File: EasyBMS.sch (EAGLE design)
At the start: 147 parts, among them Q1 BSS308PEH6327XTSA1, Q10 BSS308PEH6327XTSA1, Q11 BSS308PEH6327XTSA1, Q12 BSS308PEH6327XTSA1, Q14 BSS308PEH6327XTSA1, Q3 BSS308PEH6327XTSA1, Q4 BSS308PEH6327XTSA1, Q5 BSS308PEH6327XTSA1, Q6 BSS308PEH6327XTSA1, Q7 BSS308PEH6327XTSA1, Q8 BSS308PEH6327XTSA1, Q9 BSS308PEH6327XTSA1

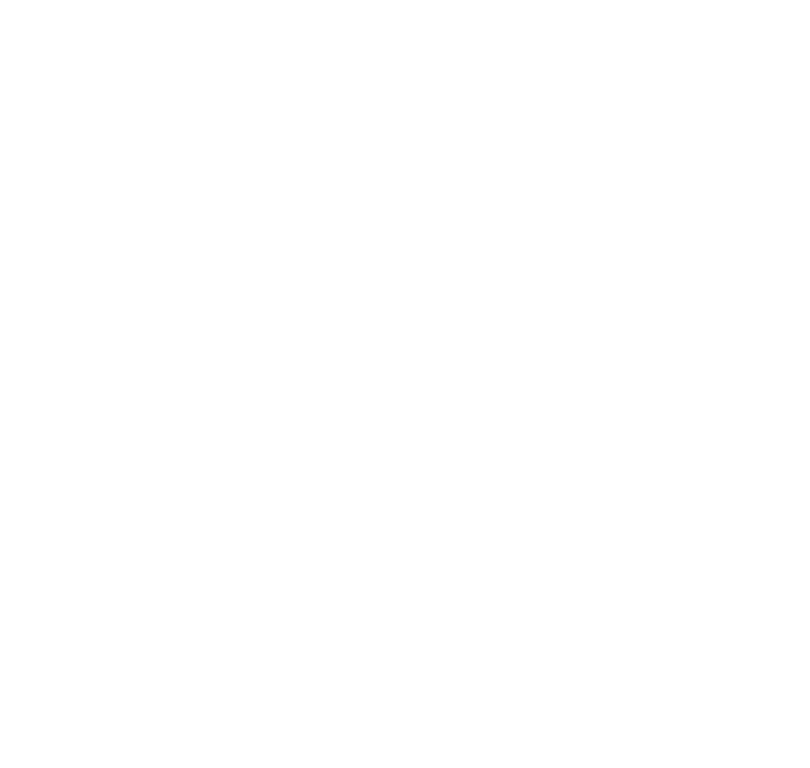
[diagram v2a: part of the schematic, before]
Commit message: shortconnection pinable between the C ports for emtpy cells
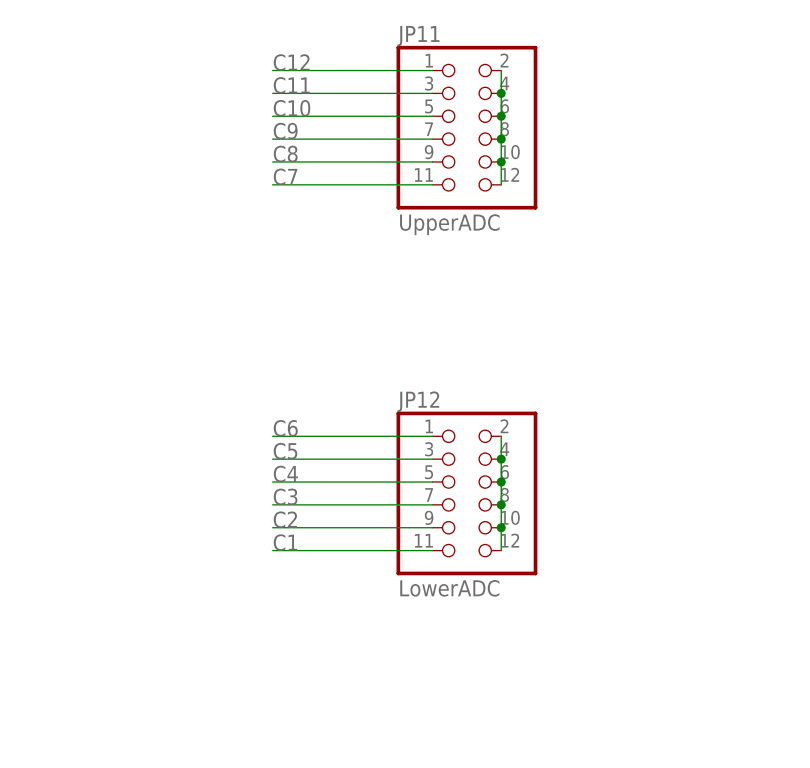
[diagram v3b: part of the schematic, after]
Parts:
- added JP11: UpperADC, pinhead:PINHD-2X6
- added JP12: LowerADC, pinhead:PINHD-2X6
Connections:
- new net N$106: JP12.10, JP12.12, JP12.2, JP12.4, JP12.6, JP12.8
- new net N$121: JP11.10, JP11.12, JP11.2, JP11.4, JP11.6, JP11.8
- net C1: now also JP12.11
- net C10: now also JP11.5
- net C11: now also JP11.3
- net C12: now also JP11.1
- net C2: now also JP12.9
- net C3: now also JP12.7
- net C4: now also JP12.5
- net C5: now also JP12.3
- net C6: now also JP12.1
- net C7: now also JP11.11
- net C8: now also JP11.9
- net C9: now also JP11.7
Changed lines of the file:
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@@
 <part name="D2" library="SamacSys_Parts" deviceset="SM4007PL-TP" device=""/>
 <part name="D3" library="SamacSys_Parts" deviceset="SM4007PL-TP" device=""/>
+<part name="JP11" library="pinhead" library_urn="urn:adsk.eagle:library:325" deviceset="PINHD-2X6" device="" package3d_urn="urn:adsk.eagle:package:22474/2" value="UpperADC"/>
+<part name="JP12" library="pinhead" library_urn="urn:adsk.eagle:library:325" deviceset="PINHD-2X6" device="" package3d_urn="urn:adsk.eagle:package:22474/2" value="LowerADC"/>
 </parts>
 <sheets>
@@
 <attribute name="NAME" x="-414.02" y="69.85" size="1.778" layer="95" rot="R270" align="center-left"/>
 <attribute name="VALUE" x="-416.56" y="69.85" size="1.778" layer="96" rot="R270" align="center-left"/>
+</instance>
+<instance part="JP11" gate="A" x="-50.8" y="726.44" smashed="yes">
+<attribute name="NAME" x="-57.15" y="734.695" size="1.778" layer="95"/>
+<attribute name="VALUE" x="-57.15" y="713.74" size="1.778" layer="96"/>
+</instance>
+<instance part="JP12" gate="A" x="-50.8" y="685.8" smashed="yes">
+<attribute name="NAME" x="-57.15" y="694.055" size="1.778" layer="95"/>
+<attribute name="VALUE" x="-57.15" y="673.1" size="1.778" layer="96"/>
 </instance>
 </instances>
@@
 <label x="-180.34" y="86.36" size="1.778" layer="95"/>
 </segment>
+<segment>
+<pinref part="JP12" gate="A" pin="11"/>
+<wire x1="-53.34" y1="678.18" x2="-71.12" y2="678.18" width="0.1524" layer="91"/>
+<label x="-71.12" y="678.18" size="1.778" layer="95"/>
+</segment>
 </net>
 <net name="S2" class="0">
@@
 <label x="-180.34" y="137.16" size="1.778" layer="95"/>
 </segment>
+<segment>
+<pinref part="JP12" gate="A" pin="9"/>
+<wire x1="-53.34" y1="680.72" x2="-71.12" y2="680.72" width="0.1524" layer="91"/>
+<label x="-71.12" y="680.72" size="1.778" layer="95"/>
+</segment>
 </net>
 <net name="S3" class="0">
@@
 <label x="-180.34" y="182.88" size="1.778" layer="95"/>
 </segment>
+<segment>
+<pinref part="JP12" gate="A" pin="7"/>
+<wire x1="-53.34" y1="683.26" x2="-71.12" y2="683.26" width="0.1524" layer="91"/>
+<label x="-71.12" y="683.26" size="1.778" layer="95"/>
+</segment>
 </net>
 <net name="S4" class="0">
@@
 <label x="-180.34" y="231.14" size="1.778" layer="95"/>
 </segment>
+<segment>
+<pinref part="JP12" gate="A" pin="5"/>
+<wire x1="-53.34" y1="685.8" x2="-71.12" y2="685.8" width="0.1524" layer="91"/>
+<label x="-71.12" y="685.8" size="1.778" layer="95"/>
+</segment>
 </net>
 <net name="S5" class="0">
@@
 <label x="-180.34" y="276.86" size="1.778" layer="95"/>
 </segment>
+<segment>
+<pinref part="JP12" gate="A" pin="3"/>
+<wire x1="-53.34" y1="688.34" x2="-71.12" y2="688.34" width="0.1524" layer="91"/>
+<label x="-71.12" y="688.34" size="1.778" layer="95"/>
+</segment>
 </net>
 <net name="S6" class="0">
@@
 <label x="-180.34" y="320.04" size="1.778" layer="95"/>
 </segment>
+<segment>
+<pinref part="JP12" gate="A" pin="1"/>
+<wire x1="-53.34" y1="690.88" x2="-71.12" y2="690.88" width="0.1524" layer="91"/>
+<label x="-71.12" y="690.88" size="1.778" layer="95"/>
+</segment>
 </net>
 <net name="S7" class="0">
@@
 <label x="-180.34" y="363.22" size="1.778" layer="95"/>
 </segment>
+<segment>
+<pinref part="JP11" gate="A" pin="11"/>
+<wire x1="-53.34" y1="718.82" x2="-71.12" y2="718.82" width="0.1524" layer="91"/>
+<label x="-71.12" y="718.82" size="1.778" layer="95"/>
+</segment>
 </net>
 <net name="S8" class="0">
@@
 <label x="-180.34" y="414.02" size="1.778" layer="95"/>
 </segment>
+<segment>
+<pinref part="JP11" gate="A" pin="9"/>
+<wire x1="-53.34" y1="721.36" x2="-71.12" y2="721.36" width="0.1524" layer="91"/>
+<label x="-71.12" y="721.36" size="1.778" layer="95"/>
+</segment>
 </net>
 <net name="S9" class="0">
@@
 <label x="-180.34" y="459.74" size="1.778" layer="95"/>
 </segment>
+<segment>
+<pinref part="JP11" gate="A" pin="7"/>
+<wire x1="-53.34" y1="723.9" x2="-71.12" y2="723.9" width="0.1524" layer="91"/>
+<label x="-71.12" y="723.9" size="1.778" layer="95"/>
+</segment>
 </net>
 <net name="S10" class="0">
@@
 <label x="-180.34" y="502.92" size="1.778" layer="95"/>
 </segment>
+<segment>
+<pinref part="JP11" gate="A" pin="5"/>
+<wire x1="-53.34" y1="726.44" x2="-71.12" y2="726.44" width="0.1524" layer="91"/>
+<label x="-71.12" y="726.44" size="1.778" layer="95"/>
+</segment>
 </net>
 <net name="S11" class="0">
@@
 <label x="-180.34" y="551.18" size="1.778" layer="95"/>
 </segment>
+<segment>
+<pinref part="JP11" gate="A" pin="3"/>
+<wire x1="-53.34" y1="728.98" x2="-71.12" y2="728.98" width="0.1524" layer="91"/>
+<label x="-71.12" y="728.98" size="1.778" layer="95"/>
+</segment>
 </net>
 <net name="S12" class="0">
@@
 <pinref part="R81" gate="G$1" pin="1"/>
 <label x="-180.34" y="596.9" size="1.778" layer="95"/>
+</segment>
+<segment>
+<pinref part="JP11" gate="A" pin="1"/>
+<wire x1="-53.34" y1="731.52" x2="-71.12" y2="731.52" width="0.1524" layer="91"/>
+<label x="-71.12" y="731.52" size="1.778" layer="95"/>
 </segment>
 </net>
@@
 </segment>
 </net>
+<net name="N$106" class="0">
+<segment>
+<pinref part="JP12" gate="A" pin="2"/>
+<pinref part="JP12" gate="A" pin="4"/>
+<wire x1="-45.72" y1="690.88" x2="-45.72" y2="688.34" width="0.1524" layer="91"/>
+<pinref part="JP12" gate="A" pin="6"/>
+<wire x1="-45.72" y1="688.34" x2="-45.72" y2="685.8" width="0.1524" layer="91"/>
+<junction x="-45.72" y="688.34"/>
+<pinref part="JP12" gate="A" pin="8"/>
+<wire x1="-45.72" y1="685.8" x2="-45.72" y2="683.26" width="0.1524" layer="91"/>
+<junction x="-45.72" y="685.8"/>
+<pinref part="JP12" gate="A" pin="10"/>
+<wire x1="-45.72" y1="683.26" x2="-45.72" y2="680.72" width="0.1524" layer="91"/>
+<junction x="-45.72" y="683.26"/>
+<pinref part="JP12" gate="A" pin="12"/>
+<wire x1="-45.72" y1="680.72" x2="-45.72" y2="678.18" width="0.1524" layer="91"/>
+<junction x="-45.72" y="680.72"/>
+</segment>
+</net>
+<net name="N$121" class="0">
+<segment>
+<pinref part="JP11" gate="A" pin="2"/>
+<pinref part="JP11" gate="A" pin="4"/>
+<wire x1="-45.72" y1="731.52" x2="-45.72" y2="728.98" width="0.1524" layer="91"/>
+<pinref part="JP11" gate="A" pin="6"/>
+<wire x1="-45.72" y1="728.98" x2="-45.72" y2="726.44" width="0.1524" layer="91"/>
+<junction x="-45.72" y="728.98"/>
+<pinref part="JP11" gate="A" pin="8"/>
+<wire x1="-45.72" y1="726.44" x2="-45.72" y2="723.9" width="0.1524" layer="91"/>
+<junction x="-45.72" y="726.44"/>
+<pinref part="JP11" gate="A" pin="10"/>
+<wire x1="-45.72" y1="723.9" x2="-45.72" y2="721.36" width="0.1524" layer="91"/>
+<junction x="-45.72" y="723.9"/>
+<pinref part="JP11" gate="A" pin="12"/>
+<wire x1="-45.72" y1="721.36" x2="-45.72" y2="718.82" width="0.1524" layer="91"/>
+<junction x="-45.72" y="721.36"/>
+</segment>
+</net>

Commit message: some caps got new values
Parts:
- added C16, C21: 100nF, rcl:C-EUC1206
- added R4: 100R, rcl:R-EU_R0402
- C10, C11, C12, C13, C14, C15, C17, C4, C5, C6, C7, C8, C9: value (none) -> 10nF
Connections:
- new net V+: C21.1, JP5.1, R4.1
- net GND: now also C16.2, C21.2
- net P13: now also R4.2; no longer JP5.1
- net VREG: now also C16.1
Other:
- moved on the sheet: C1, C10, C11, C12, C13, C14, C15, C17, C2, C3, C4, C5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

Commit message: MOSFETS changed to a available Type
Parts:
- added C18, C19: 100nF, rcl:C-EUC1206
- Q1, Q10, Q11, Q12, Q14, Q3, Q4, Q5, Q6, Q7, Q8, Q9: value BSS308PEH6327XTSA1 -> C8547
- R5: device rcl:R-EU_R0603 -> rcl:R-EU_R0402
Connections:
- net 5VDC: no longer C3.+
- net GND: now also C18.2, C19.2
- net VREF1: now also C18.1
- net VREF2: now also C19.1
- net VREG: now also C3.+
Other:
- moved on the sheet: C1, C3

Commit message: layouted
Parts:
- removed C6: 10nF, rcl:C-EUC0402
- removed LED18, LED6: KT-0603R, led:LEDCHIPLED_0603
- removed Q14, Q3: C8547, SamacSys_Parts:BSS308PEH6327XTSA1
- removed R100, R23: 100R, rcl:R-EU_R0402
- removed R12, R14, R20, R97: 10R0, rcl:R-EU_R1206
- removed R21, R98: 3.3k, rcl:R-EU_R0402
- removed R22, R99: 470R, rcl:R-EU_R0402
- added C20: 10nF, rcl:C-EUC0402
- added LED17, LED5: KT-0603R, led:LEDCHIPLED_0603
- added Q13, Q2: C8547, SamacSys_Parts:BSS308PEH6327XTSA1
- added R10, R94: 3.3k, rcl:R-EU_R0402
- added R11, R89: 470R, rcl:R-EU_R0402
- added R7, R8, R91, R92, R93: 10R0, rcl:R-EU_R1206
- added R90: 100R, rcl:R-EU_R0402
- R13: value 3.3k -> 100R
- R19, R29, R35, R41, R47, R63, R69, R75, R81: value 100R -> 10R0; device rcl:R-EU_R0402 -> rcl:R-EU_R1206
- R24, R30, R36, R42, R48, R64, R70, R76: value 10R0 -> 3.3k; device rcl:R-EU_R1206 -> rcl:R-EU_R0402
- R25, R31, R37, R43, R49, R65, R71, R77, R83, R95: value 10R0 -> 470R; device rcl:R-EU_R1206 -> rcl:R-EU_R0402
- R26, R32, R38, R44, R50, R66, R72, R78, R84, R96: value 10R0 -> 100R; device rcl:R-EU_R1206 -> rcl:R-EU_R0402
- R27, R33, R39, R45, R51, R67, R73, R79, R86: value 3.3k -> 10R0; device rcl:R-EU_R0402 -> rcl:R-EU_R1206
- R28, R34, R40, R46, R52, R68, R74, R80, R87: value 470R -> 10R0; device rcl:R-EU_R0402 -> rcl:R-EU_R1206
- R82: value 470R -> 3.3k
- R88: value 100R -> 3.3k
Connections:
- removed net N$14: R12.2, R14.1
- removed net N$15: R18.2, R9.1
- removed net N$157: LED10.C, R82.1
- removed net N$16: R14.2, R20.1
- removed net N$19: LED6.A, Q3.D, R20.2
- removed net N$20: Q3.G, R21.2
- removed net N$22: LED6.C, R22.1
- removed net N$27 (its old number): LED7.A, Q4.D, R26.2
- new net N$122: Q12.G, R88.2
- new net N$123: LED16.C, R89.1
- new net N$125: R91.2, R92.1
- new net N$126: R92.2, R93.1
- new net N$127: LED17.A, Q13.D, R93.2
- new net N$128: Q13.G, R94.2
- new net N$129: LED17.C, R95.1
- new net N$17: R7.2, R8.1
- net C1: now also R13.1; no longer R19.1
- net C10: now also C15.1, R84.1; no longer C17.1, R100.1
- net C11: now also C17.1, R90.1; no longer C12.1, R69.1
- net C12: now also C20.1, R96.1; no longer C14.1, R81.1
- net C2: now also C8.1, R32.1; no longer C6.1, R23.1
- net C3: now also R26.1; no longer R29.1
- net C4: now also C9.1, R38.1; no longer C8.1, R35.1
- net C5: now also C10.1, R44.1; no longer C9.1, R41.1
- net C6: now also C11.1, R50.1; no longer C10.1, R47.1
- net C7: now also C12.1, R66.1; no longer C11.1, R63.1
- net C8: now also R72.1; no longer R75.1
- net C9: now also C14.1, R78.1; no longer C15.1, R88.1
- net GND: now also R11.2, R7.1; no longer R17.1, R82.2
- net N$18: now also R8.2, R9.1; no longer LED10.A, Q1.D, R9.2
- net N$23: now also LED5.A, Q1.D, R9.2; no longer R24.2, R25.1
- net N$25: now also R10.2; no longer R13.2
- net N$26: now also LED5.C, R11.1; no longer R25.2, R26.1
- net N$28: now also R18.2, R19.1; no longer Q4.G, R27.2
- net N$29: now also LED7.A, Q2.D, R19.2; no longer LED7.C, R28.1
- net N$31: now also Q2.G, R24.2; no longer R30.2, R31.1
- net N$32: now also LED7.C, R25.1; no longer R31.2, R32.1
- net N$33: now also R27.2, R28.1; no longer LED8.A, Q5.D, R32.2
- net N$34: now also R28.2, R29.1; no longer Q5.G, R33.2
- net N$35: now also LED8.A, Q4.D, R29.2; no longer LED8.C, R34.1
- net N$36: now also Q4.G, R30.2; no longer R36.2, R37.1
- net N$37: now also LED8.C, R31.1; no longer R37.2, R38.1
- net N$38: now also R33.2, R34.1; no longer LED9.A, Q6.D, R38.2
- net N$39: now also R34.2, R35.1; no longer Q6.G, R39.2
- net N$40: now also LED9.A, Q5.D, R35.2; no longer LED9.C, R40.1
- net N$41: now also Q5.G, R36.2; no longer R42.2, R43.1
- net N$42: now also LED9.C, R37.1; no longer R43.2, R44.1
- net N$43: now also R39.2, R40.1; no longer LED11.A, Q7.D, R44.2
- net N$44: now also R40.2, R41.1; no longer Q7.G, R45.2
- net N$45: now also LED10.A, Q6.D, R41.2; no longer LED11.C, R46.1
- net N$46: now also Q6.G, R42.2; no longer R48.2, R49.1
- net N$47: now also LED10.C, R43.1; no longer R49.2, R50.1
- net N$48: now also R45.2, R46.1; no longer LED12.A, Q8.D, R50.2
- net N$49: now also R46.2, R47.1; no longer Q8.G, R51.2
- net N$50: now also LED11.A, Q7.D, R47.2; no longer LED12.C, R52.1
- net N$51: now also Q7.G, R48.2; no longer R64.2, R65.1
- net N$52: now also LED11.C, R49.1; no longer R65.2, R66.1
- net N$53: now also R51.2, R52.1; no longer LED13.A, Q9.D, R66.2
- net N$54: now also R52.2, R63.1; no longer Q9.G, R67.2
- net N$55: now also LED12.A, Q8.D, R63.2; no longer LED13.C, R68.1
- net N$56: now also Q8.G, R64.2; no longer R70.2, R71.1
- net N$57: now also LED12.C, R65.1; no longer R71.2, R72.1
- net N$58: now also R67.2, R68.1; no longer LED14.A, Q10.D, R72.2
- net N$59: now also R68.2, R69.1; no longer Q10.G, R73.2
- net N$60: now also LED13.A, Q9.D, R69.2; no longer LED14.C, R74.1
- net N$62: now also Q9.G, R70.2; no longer R76.2, R77.1
- net N$63: now also LED13.C, R71.1; no longer R77.2, R78.1
- net N$64: now also R73.2, R74.1; no longer LED15.A, Q11.D, R78.2
- net N$65: now also R74.2, R75.1; no longer Q11.G, R79.2
- net N$66: now also LED14.A, Q10.D, R75.2; no longer LED15.C, R80.1
- net N$67: now also Q10.G, R76.2; no longer R83.2, R84.1
- net N$68: now also LED14.C, R77.1; no longer R84.2, R85.1
- net N$69: now also R79.2, R80.1; no longer LED16.A, Q12.D, R85.2
- net N$71: now also R80.2, R81.1; no longer Q12.G, R86.2
- net N$72: now also LED15.A, Q11.D, R81.2; no longer LED16.C, R87.1
- net N$79: now also Q11.G, R82.2; no longer R95.2, R96.1
- net N$80: now also LED15.C, R83.1; no longer R96.2, R97.1
- net N$81: now also R85.2, R86.1; no longer LED18.A, Q14.D, R97.2
- net N$82: now also R86.2, R87.1; no longer Q14.G, R98.2
- net N$83: now also LED16.A, Q12.D, R87.2; no longer LED18.C, R99.1
- net P10: now also C15.2, Q10.S, R78.2, R79.1, R83.2; no longer C17.2, Q12.S, R88.2, R95.1, R99.2
- net P11: now also C17.2, Q11.S, R84.2, R85.1, R89.2; no longer C12.2, Q14.S, R100.2, R64.1, R68.2
- net P12: now also C20.2, Q12.S, R90.2, R91.1, R95.2; no longer C14.2, Q9.S, R69.2, R76.1, R80.2
- net P13: now also Q13.S, R96.2; no longer Q11.S, R81.2
- net P2: now also C8.2, R13.2, R27.1, R31.2; no longer C6.2, R12.1, R19.2, R22.2
- net P3: now also Q4.S, R17.1, R25.2, R32.2; no longer Q3.S, R23.2, R24.1, R28.2
- net P4: now also C9.2, Q2.S, R26.2, R33.1, R37.2; no longer C8.2, Q4.S, R29.2, R30.1, R34.2
- net P5: now also C10.2, R38.2, R39.1, R43.2; no longer C9.2, R35.2, R36.1, R40.2
- net P6: now also C11.2, R44.2, R45.1, R49.2; no longer C10.2, R41.2, R42.1, R46.2
- net P7: now also C12.2, R50.2, R51.1, R65.2; no longer C11.2, R47.2, R48.1, R52.2
- net P8: now also R66.2, R67.1, R71.2; no longer R63.2, R70.1, R74.2
- net P9: now also C14.2, Q9.S, R72.2, R73.1, R77.2; no longer C15.2, Q10.S, R75.2, R83.1, R87.2
- net S1: now also R10.1; no longer R13.1
- net S10: now also R82.1; no longer R98.1
- net S11: now also R88.1; no longer R67.1
- net S12: now also R94.1; no longer R79.1
- net S2: now also R30.1; no longer R21.1
- net S3: now also R24.1; no longer R27.1
- net S4: now also R36.1; no longer R33.1
- net S5: now also R42.1; no longer R39.1
- net S6: now also R48.1; no longer R45.1
- net S7: now also R64.1; no longer R51.1
- net S8: now also R70.1; no longer R73.1
- net S9: now also R76.1; no longer R86.1
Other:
- moved on the sheet: C10, C11, C12, C13, C14, C15, C17, C4, C5, C7, C8, C9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
